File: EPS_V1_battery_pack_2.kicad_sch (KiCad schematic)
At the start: 33 parts, among them U1 MP2672AGD-0000-Z, U5 MAX17205G+

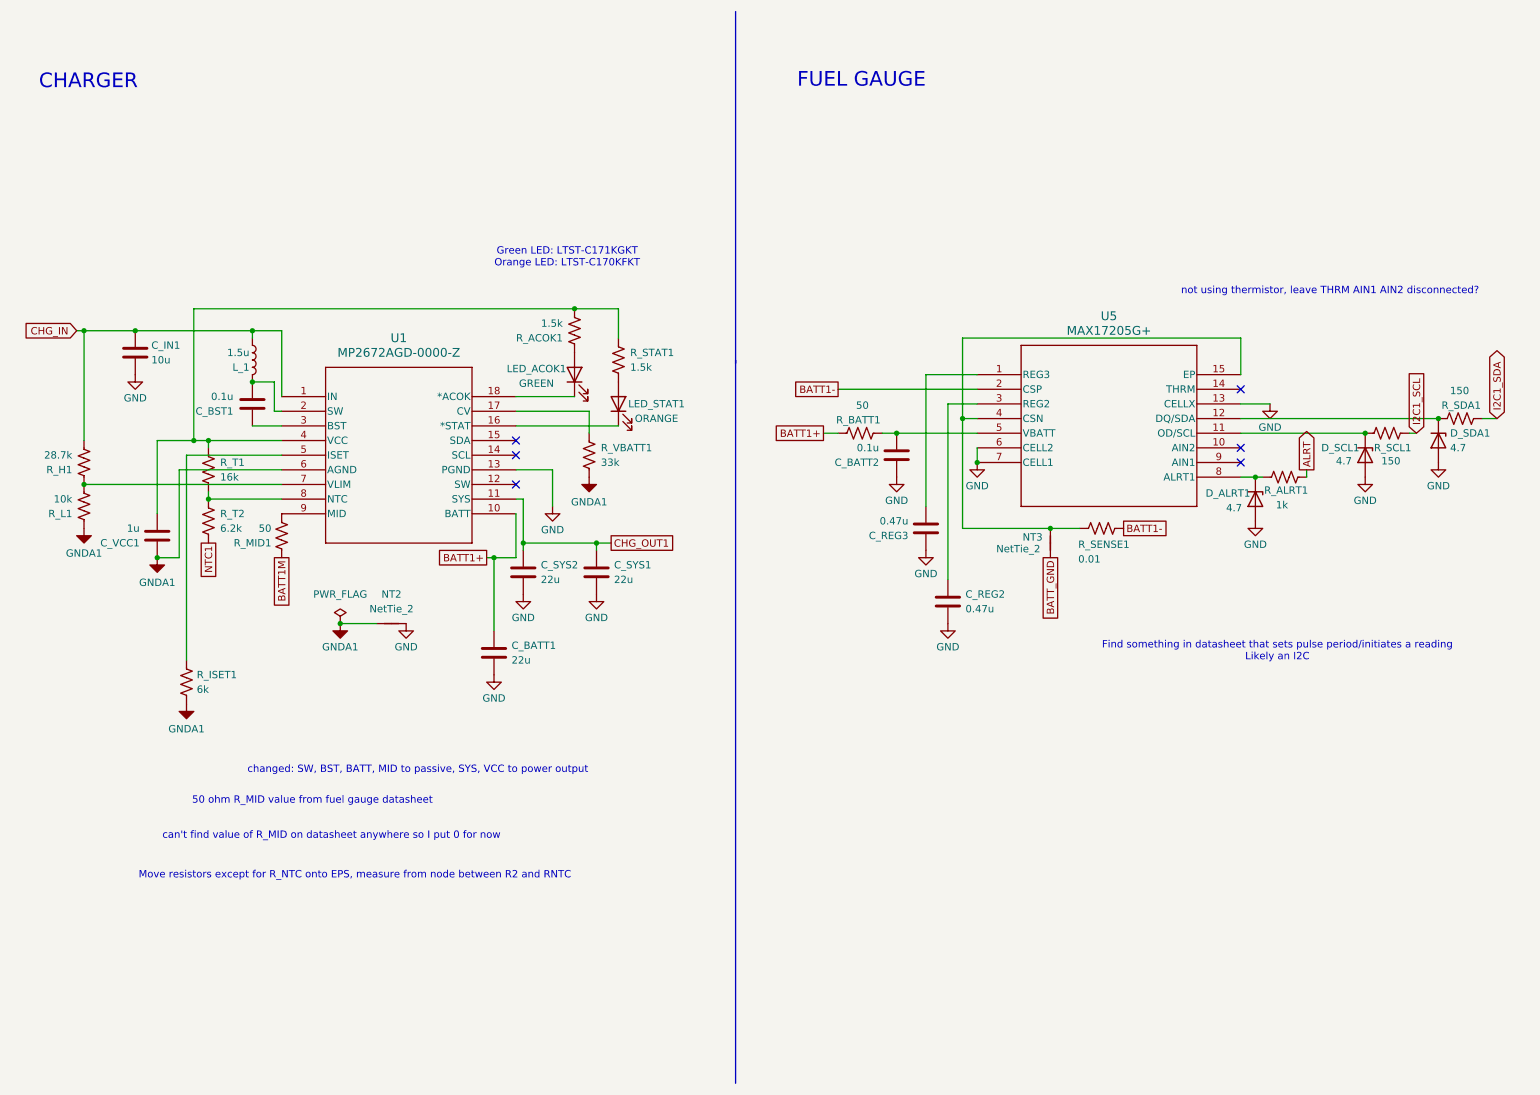
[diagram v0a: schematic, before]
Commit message: Add other battery packs, connect all ALRT signals, assign footprints for new components, make inhibit switch footprints
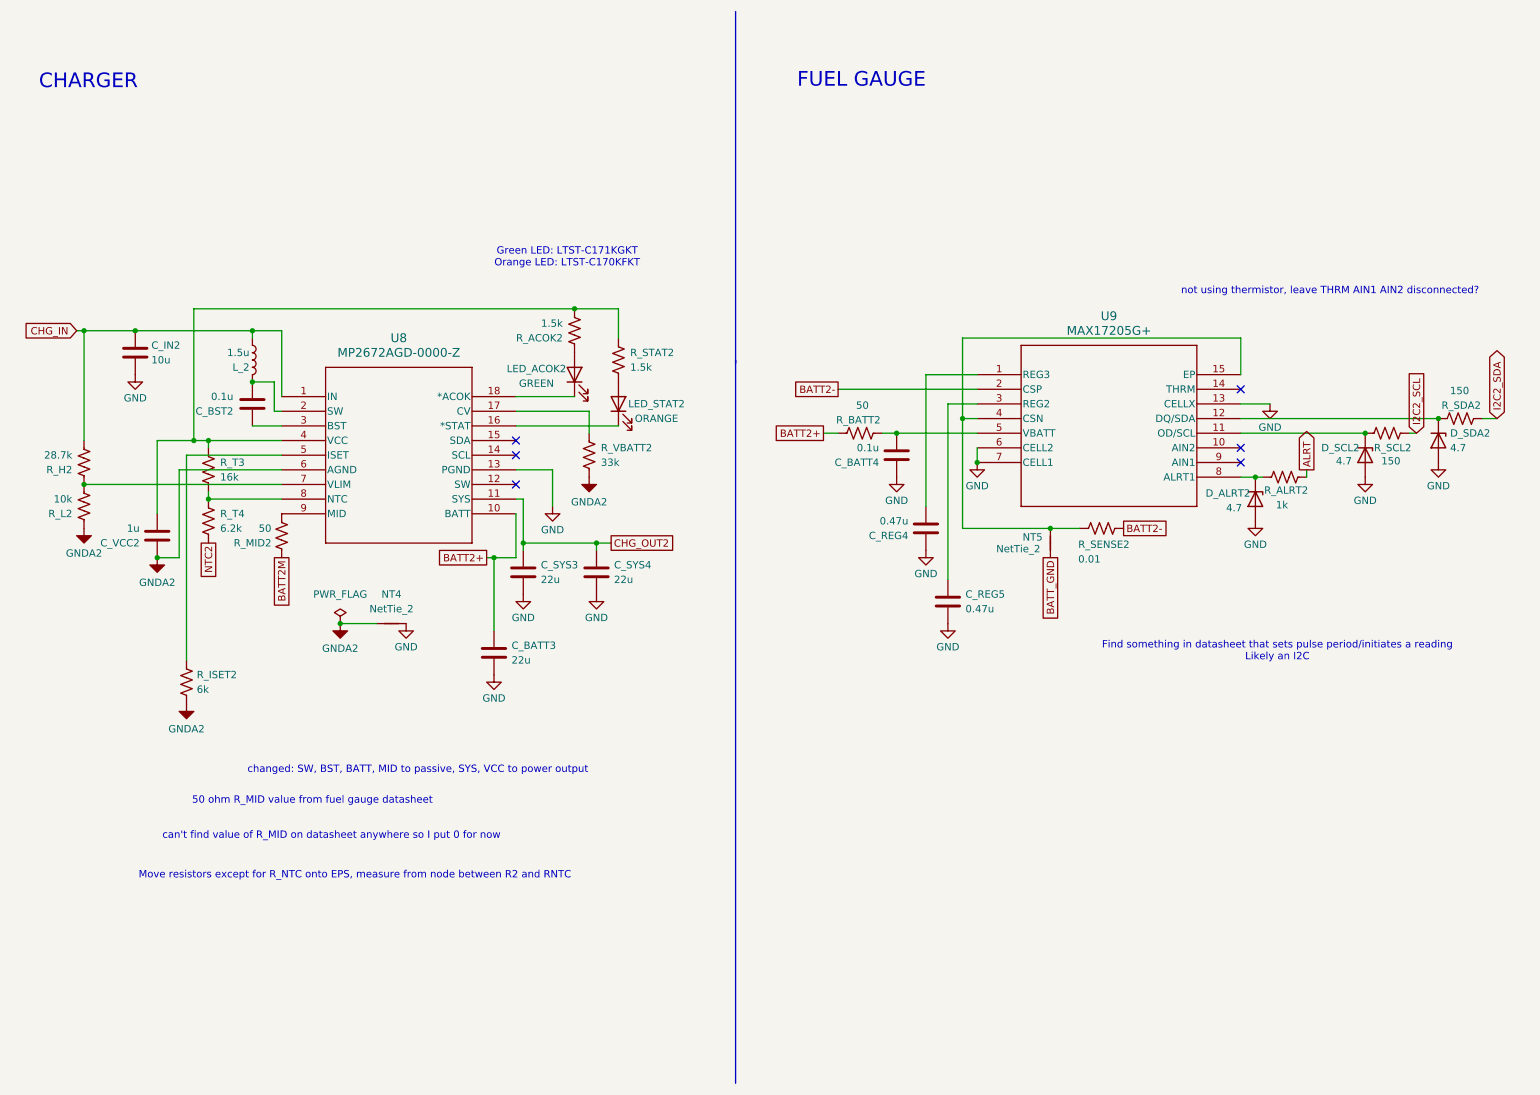
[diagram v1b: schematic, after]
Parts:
- removed C_BATT1, C_SYS1, C_SYS2: 22u, Capacitor_SMD:C_0805_2012Metric, symbol Device:C
- removed C_BATT2, C_BST1: 0.1u, Capacitor_SMD:C_0603_1608Metric, symbol Device:C
- removed C_IN1: 10u, Capacitor_SMD:C_0805_2012Metric, symbol Device:C
- removed C_REG2, C_REG3: 0.47u, Capacitor_SMD:C_0603_1608Metric, symbol Device:C
- removed C_VCC1: 1u, Capacitor_SMD:C_0603_1608Metric, symbol Device:C
- removed D_ALRT1, D_SCL1, D_SDA1: 4.7, Diode_SMD:D_0603_1608Metric, symbol Device:D_Zener
- removed LED_ACOK1: GREEN, LED_SMD:LED_0805_2012Metric, symbol Device:LED
- removed LED_STAT1: ORANGE, LED_SMD:LED_0805_2012Metric, symbol Device:LED
- removed L_1: 1.5u, AMELA2012S_1R5MT:IND_AMELA2012S-1R5MT, symbol Device:L
- removed NT2, NT3: NetTie_2, NetTie:NetTie-2_SMD_Pad2.0mm, symbol Device:NetTie_2
- removed R_ACOK1, R_STAT1: 1.5k, Resistor_SMD:R_0603_1608Metric, symbol Device:R_US
- removed R_ALRT1: 1k, Resistor_SMD:R_0603_1608Metric, symbol Device:R_US
- removed R_BATT1, R_MID1: 50, Resistor_SMD:R_0603_1608Metric, symbol Device:R_US
- removed R_H1: 28.7k, Resistor_SMD:R_0603_1608Metric, symbol Device:R_US
- removed R_ISET1: 6k, Resistor_SMD:R_0603_1608Metric, symbol Device:R_US
- removed R_L1: 10k, Resistor_SMD:R_0603_1608Metric, symbol Device:R_US
- removed R_SCL1, R_SDA1: 150, Resistor_SMD:R_0603_1608Metric, symbol Device:R_US
- removed R_SENSE1: 0.01, Resistor_SMD:R_0603_1608Metric, symbol Device:R_US
- removed R_T1: 16k, Resistor_SMD:R_0603_1608Metric, symbol Device:R_US
- removed R_T2: 6.2k, Resistor_SMD:R_0603_1608Metric, symbol Device:R_US
- removed R_VBATT1: 33k, Resistor_SMD:R_0603_1608Metric, symbol Device:R_US
- removed U1: MP2672AGD-0000-Z, MP2672AGD_0000_Z:QFN-18_MP2672A_MNP, symbol 2026-04-14_17-23-40:MP2672AGD-0000-Z
- removed U5: MAX17205G+, MAX17205G:21-0137_T1433&plus_2C_MXM, symbol MAX17205G:MAX17205G+
- added C_BATT3, C_SYS3, C_SYS4: 22u, Capacitor_SMD:C_0805_2012Metric, symbol Device:C
- added C_BATT4, C_BST2: 0.1u, Capacitor_SMD:C_0603_1608Metric, symbol Device:C
- added C_IN2: 10u, Capacitor_SMD:C_0805_2012Metric, symbol Device:C
- added C_REG4, C_REG5: 0.47u, Capacitor_SMD:C_0603_1608Metric, symbol Device:C
- added C_VCC2: 1u, Capacitor_SMD:C_0603_1608Metric, symbol Device:C
- added D_ALRT2, D_SCL2, D_SDA2: 4.7, Diode_SMD:D_0603_1608Metric, symbol Device:D_Zener
- added LED_ACOK2: GREEN, LED_SMD:LED_0805_2012Metric, symbol Device:LED
- added LED_STAT2: ORANGE, LED_SMD:LED_0805_2012Metric, symbol Device:LED
- added L_2: 1.5u, AMELA2012S_1R5MT:IND_AMELA2012S-1R5MT, symbol Device:L
- added NT4, NT5: NetTie_2, NetTie:NetTie-2_SMD_Pad2.0mm, symbol Device:NetTie_2
- added R_ACOK2, R_STAT2: 1.5k, Resistor_SMD:R_0603_1608Metric, symbol Device:R_US
- added R_ALRT2: 1k, Resistor_SMD:R_0603_1608Metric, symbol Device:R_US
- added R_BATT2, R_MID2: 50, Resistor_SMD:R_0603_1608Metric, symbol Device:R_US
- added R_H2: 28.7k, Resistor_SMD:R_0603_1608Metric, symbol Device:R_US
- added R_ISET2: 6k, Resistor_SMD:R_0603_1608Metric, symbol Device:R_US
- added R_L2: 10k, Resistor_SMD:R_0603_1608Metric, symbol Device:R_US
- added R_SCL2, R_SDA2: 150, Resistor_SMD:R_0603_1608Metric, symbol Device:R_US
- added R_SENSE2: 0.01, Resistor_SMD:R_0603_1608Metric, symbol Device:R_US
- added R_T3: 16k, Resistor_SMD:R_0603_1608Metric, symbol Device:R_US
- added R_T4: 6.2k, Resistor_SMD:R_0603_1608Metric, symbol Device:R_US
- added R_VBATT2: 33k, Resistor_SMD:R_0603_1608Metric, symbol Device:R_US
- added U8: MP2672AGD-0000-Z, MP2672AGD_0000_Z:QFN-18_MP2672A_MNP, symbol 2026-04-14_17-23-40:MP2672AGD-0000-Z
- added U9: MAX17205G+, MAX17205G:21-0137_T1433&plus_2C_MXM, symbol MAX17205G:MAX17205G+
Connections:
- net ALRT: now also R_ALRT2.2
- net BATT_GND: now also NT5.1
- net CHG_IN: now also C_IN2.1, L_2.1, R_H2.2, U8.1 (IN)
- net GND: now also C_BATT3.2, C_BATT4.1, C_IN2.2, C_REG4.1, C_REG5.2, C_SYS3.2, C_SYS4.2, D_ALRT2.2 (A), D_SCL2.2 (A), D_SDA2.2 (A), NT4.2, U8.13 (PGND), U9.13 (CELLX), U9.6 (CELL2), U9.7 (CELL1)
- new net: C_BST2.2, L_2.2, U8.2 (SW)
- new net: C_VCC2.2, R_ACOK2.2, R_STAT2.1, R_T3.1, U8.4 (VCC)
- new net: C_REG4.2, U9.1 (REG3)
- new net: D_SCL2.1 (K), R_SCL2.1, U9.11 (OD/SCL)
- new net: D_SDA2.1 (K), R_SDA2.1, U9.12 (DQ/SDA)
- new net: NT5.2, R_SENSE2.2, U9.15 (EP), U9.4 (CSN)
- new net: C_REG5.1, U9.3 (REG2)
- new net: C_BATT4.2, R_BATT2.2, U9.5 (VBATT)
- new net: D_ALRT2.1 (K), R_ALRT2.1, U9.8 (ALRT1)
- new net: LED_STAT2.2 (A), R_STAT2.2
- new net: C_BST2.1, U8.3 (BST)
- new net: R_MID2.2, U8.9 (MID)
- new net: LED_STAT2.1 (K), U8.16 (*STAT)
- new net: R_VBATT2.1, U8.17 (CV)
- new net: LED_ACOK2.1 (K), U8.18 (*ACOK)
- new net: R_ISET2.1, U8.5 (ISET)
- new net: R_H2.1, R_L2.2, U8.7 (VLIM)
- new net: R_T3.2, R_T4.1, U8.8 (NTC)
- new net: LED_ACOK2.2 (A), R_ACOK2.1
- new net BATT2+: C_BATT3.1, R_BATT2.1, U8.10 (BATT)
- new net BATT2-: R_SENSE2.1, U9.2 (CSP)
- new net BATT2M: R_MID2.1
- new net CHG_OUT2: C_SYS3.1, C_SYS4.1, U8.11 (SYS)
- new net GNDA2: C_VCC2.1, NT4.1, R_ISET2.2, R_L2.1, R_VBATT2.2, U8.6 (AGND)
- new net I2C2_SCL: R_SCL2.2
- new net I2C2_SDA: R_SDA2.2
- new net NTC2: R_T4.2

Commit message: Do layout draft
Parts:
- removed D_ALRT2: 4.7, Diode_SMD:D_0603_1608Metric, symbol Device:D_Zener
- removed R_ALRT2: 1k, Resistor_SMD:R_0603_1608Metric, symbol Device:R_US
- NT4, NT5: footprint NetTie:NetTie-2_SMD_Pad2.0mm -> NetTie:NetTie-2_SMD_Pad0.5mm
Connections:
- net ALRT: now also U9.8 (ALRT1)
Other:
- moved on the sheet: D_SCL2, D_SDA2, R_SCL2, R_SDA2
